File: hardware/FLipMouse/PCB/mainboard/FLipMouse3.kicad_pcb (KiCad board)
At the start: 2 copper layers, 61 x 32 mm, 78 parts, among them J1 PJ320D, J10 Conn_01x06, J13 tp, J14 tp, J15 tp, J16 tp, J17 tp, J2 PJ320D, J3 M50-3900542, J4 Conn_ARM_JTAG_SWD_10, J5 Conn_02x05_Odd_Even, J9 USB_OTG, Q1 BC847, Q2 BSH108, Q3 BC847, Q4 BSH108, Q5 BSH108, Q6 BSH108, SW1 SW_Push, SW2 SW_Push, U1 ESP32-WROOM, U2 TSOP4838, U3 LPC11U14FBD, U4 TSR_1-2433, U5 MPXV7007GP, Y1 JA-12.000-18-DFE

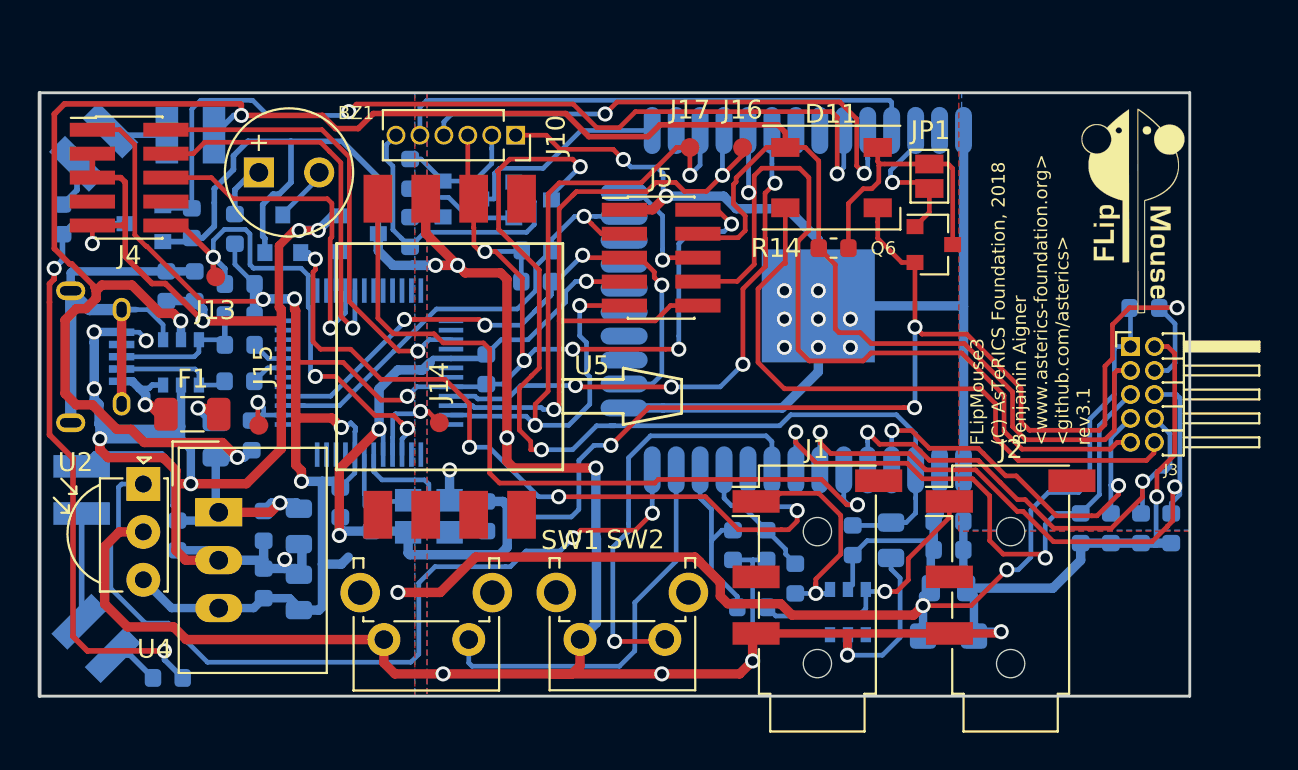
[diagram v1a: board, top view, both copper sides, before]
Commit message: Changed component names for having all part types in one order. Added 3d shapes & beautified silkscreen layers.
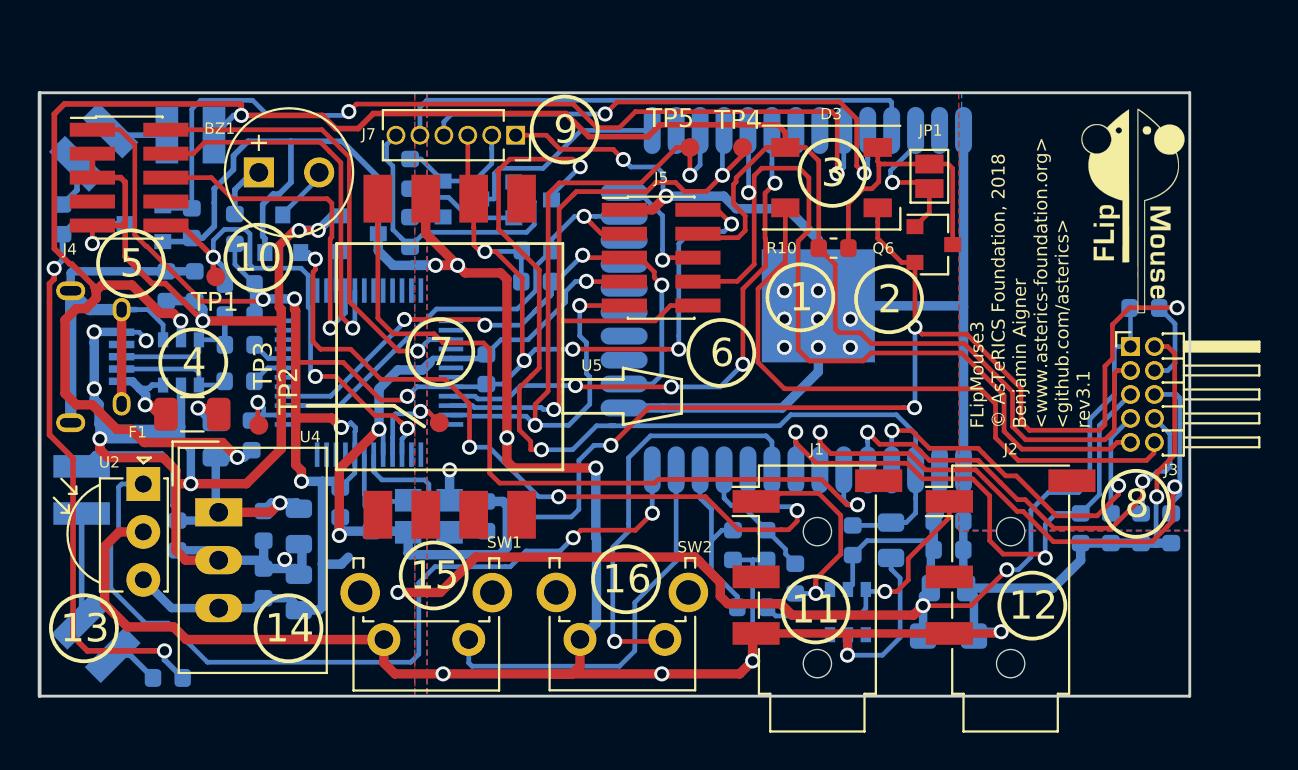
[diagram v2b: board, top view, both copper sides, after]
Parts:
- removed the C14 at (67.3, 141.5)
- removed the C2 at (96.8, 142.0)
- removed J14: tp, Measurement_Points:Measurement_Point_Round-SMD-Pad_Small
- removed the R6 at (120.0, 141.1)
- added C3: 10n, Capacitor_SMD:C_0603_1608Metric, B.Cu at (98.6, 142.0)
- added C4: 10n, Capacitor_SMD:C_0603_1608Metric, B.Cu at (96.8, 142.0)
- added R13: 10k, Resistor_SMD:R_0603_1608Metric, B.Cu at (120.0, 141.1)
- added TP2: tp, Measurement_Points:Measurement_Point_Round-SMD-Pad_Small, F.Cu at (81.2, 135.5)
- C1: value 10n -> 18pF
- C6: value 18pF -> 10n
- R6: renamed from R1; value 1.5k -> 1k5
- R7: renamed from R4; value 1.5k -> 1k5
- moved C6 16.4 mm to (67.3, 141.5)
- moved C1 14.9 mm to (83.7, 140.5), turned to 270 degrees
- renumbered C17 to C10, C23 to C11, C22 to C13, C13 to C14, C19 to C16, C10 to C17, C16 to C18, C8 to C2, C11 to C5, C18 to C7, C20 to C8, C21 to C9, D9 to D1, D3 to D2, D11 to D3, J9 to J6, J10 to J7, Q3 to Q2, Q2 to Q3, R9 to R1, R14 to R10, R17 to R11, R5 to R12, R7 to R14, R8 to R15, R11 to R16, R22 to R17, R10 to R2, R21 to R20, R20 to R21, R12 to R22, R15 to R3, R16 to R4, R3 to R5, R2 to R8, R13 to R9, J13 to TP1, J15 to TP3, J16 to TP4, J17 to TP5
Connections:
- C1 pad 1: GNDD -> GND
- C1 pad 2: /B_1 -> Net-(C1-Pad2)
- C6 pad 1: GND -> VBUS
- C6 pad 2: Net-(C6-Pad2) -> GND
- U3 pad 6: Net-(C6-Pad2) -> Net-(C1-Pad2)
- Y1 pad 1: Net-(C6-Pad2) -> Net-(C1-Pad2)
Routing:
- net Net-(C6-Pad2): track 9.64 -> 0.00 mm
- net Net-(C1-Pad2): track 0.00 -> 9.64 mm
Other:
- board text added: "1"
- board text added: "10"
- board text added: "11"
- board text added: "12"
- board text added: "13"
- board text added: "14"
- board text added: "15"
- board text added: "16"
- board text added: "2"
- board text added: "3"
- board text added: "4"
- board text added: "5"
- board text added: "6"
- board text added: "7"
- board text added: "8"
- board text added: "9"
- board text added: "FLipMouse3 © AsTeRICS Foundation, 2018 Benjamin Aigner <www.asterics-foundation.org> <github.com/asterics> rev3.1"
- board text removed: "FLipMouse3 (C) AsTeRICS Foundation, 2018 Benjamin Aigner <www.asterics-foundation.org> <github.com/asterics> rev3.1"

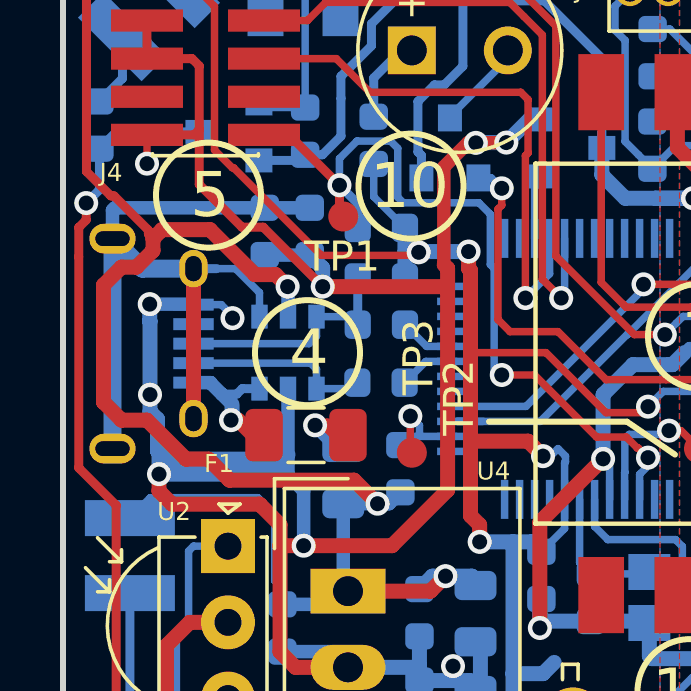
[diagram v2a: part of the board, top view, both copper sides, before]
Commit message: Changed ESD protection for VBUS
Moved the supply voltage pin of suppressor diode array
from VBUS (after fuse & ferrite bead) to the power input of
the USB plug -> ESD protection is bad with an inductor limiting
the ESD diodes.
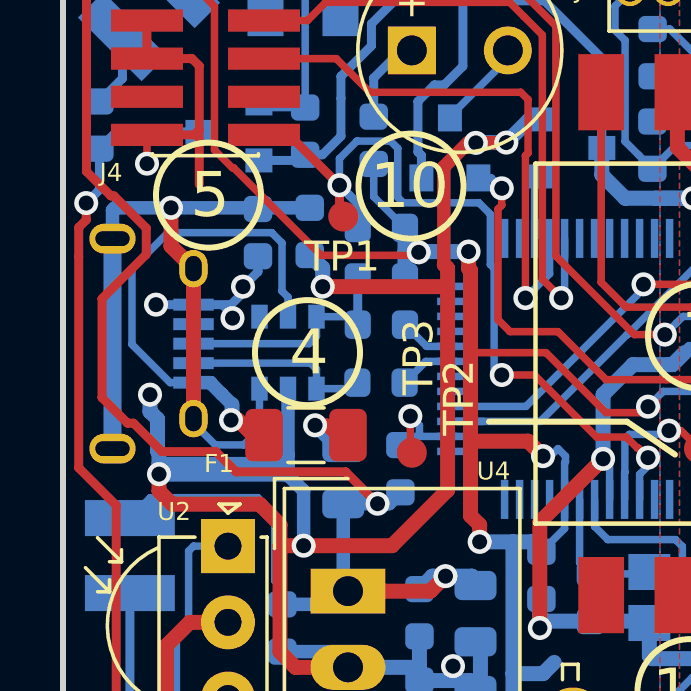
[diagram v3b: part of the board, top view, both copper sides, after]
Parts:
- moved R22 0.23 mm to (66.5, 128.3)
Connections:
- D1 pad 3: Net-(D1-Pad3) -> Net-(C5-Pad2)
- D1 pad 4: Net-(C5-Pad2) -> (no net)
- D1 pad 5: VBUS -> Net-(D1-Pad5)
- F1 pad 2: Net-(D1-Pad3) -> Net-(D1-Pad5)
- J6 pad 1: Net-(D1-Pad3) -> Net-(D1-Pad5)
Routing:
- net Net-(D1-Pad5): track 0.00 -> 16.8 mm, vias 0 -> 1
- net VBUS: track 142.5 -> 135.6 mm, vias 4 -> 3
- net GND: track 203.9 -> 197.1 mm, vias 18 -> 19
- net Net-(D1-Pad3): track 4.88 -> 0.00 mm, vias 1 -> 0
- net Net-(C5-Pad2): vias 0 -> 1

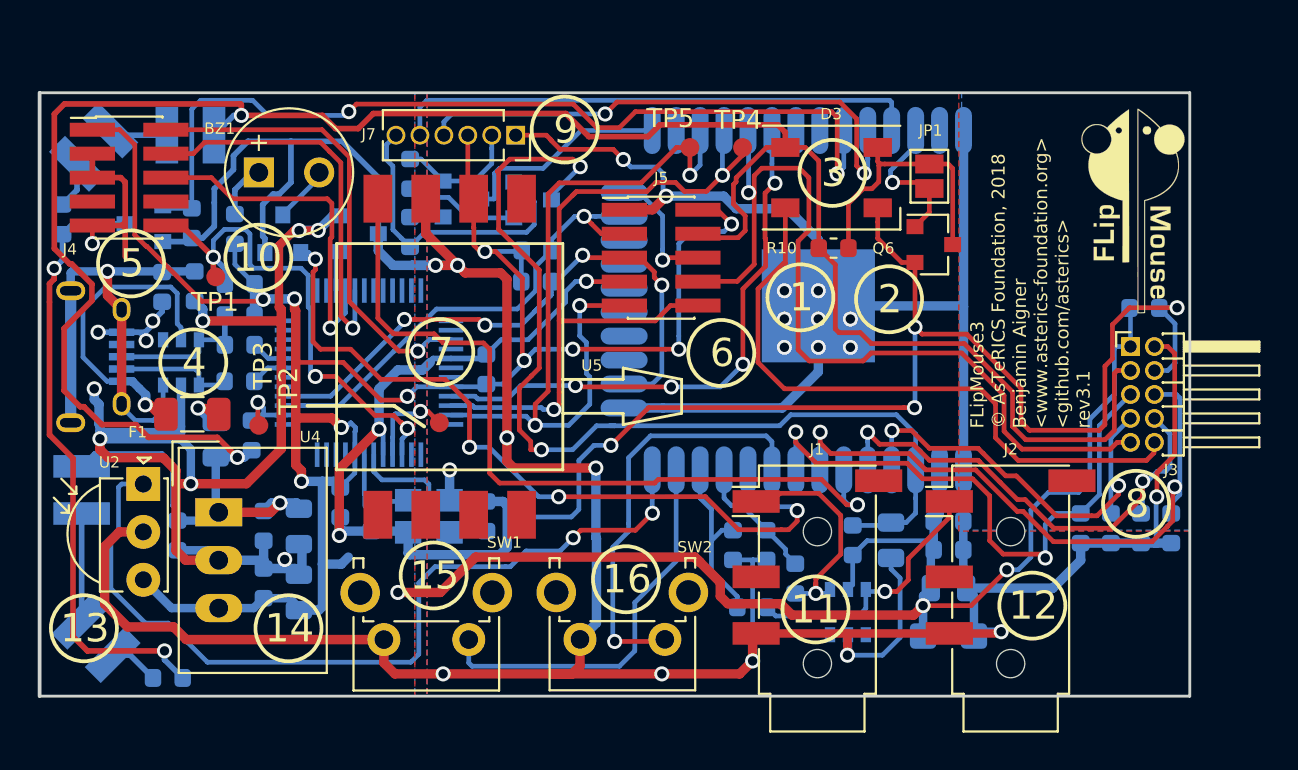
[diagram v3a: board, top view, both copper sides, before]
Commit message: Production ready, alpha: * Added marks/logos/fiducials * Changed neopixel driving * Moved RX/TX of EXT header from internal UART to free pins * Renumbered all parts for having same part types with following numbers * Added PDFs of PCB
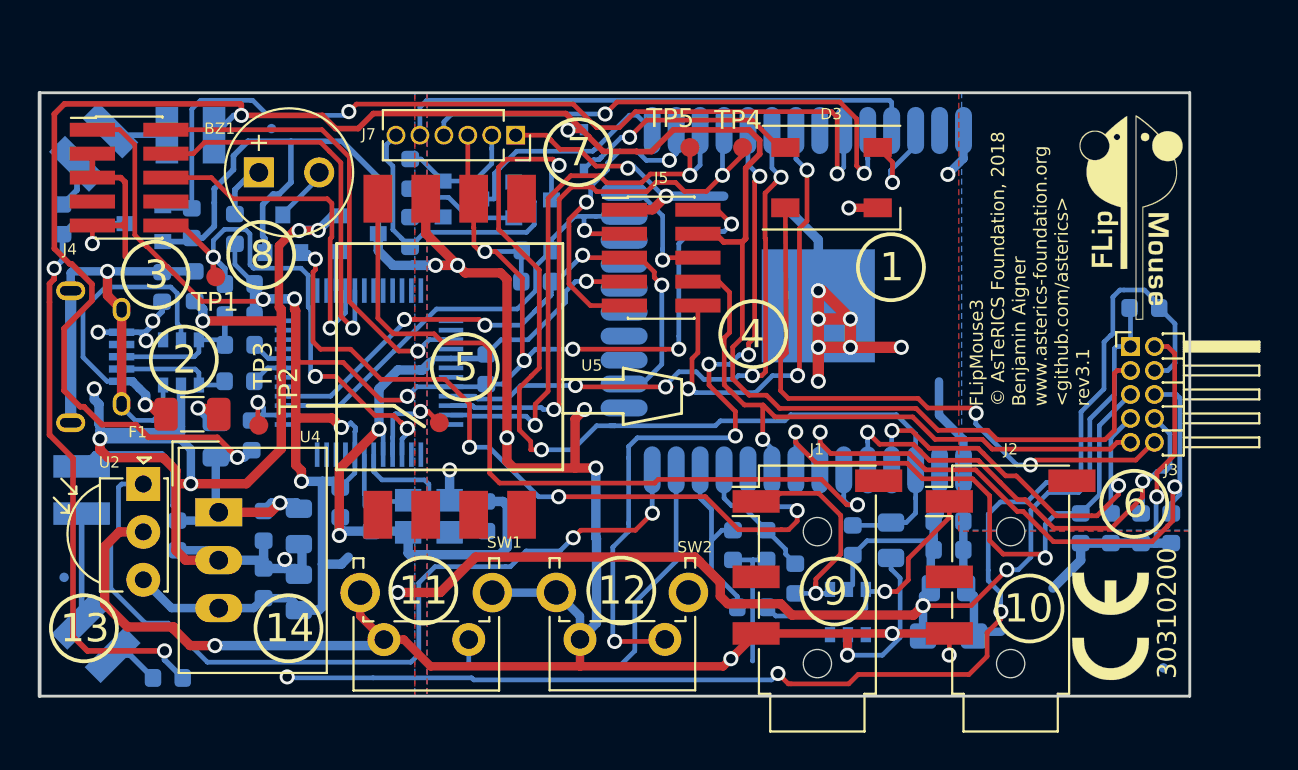
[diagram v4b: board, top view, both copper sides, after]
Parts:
- removed G***: LOGO, Logo:flipmouse_11x5
- removed JP1: IO direct, Jumper:SolderJumper-2_P1.3mm_Open_Pad1.0x1.5mm
- removed Q6: BSH108, Package_TO_SOT_SMD:SOT-23
- removed the R10 at (102.1, 126.2)
- added D8: 1N4148WS, Diode_SMD:D_SOD-323, B.Cu at (88.9, 121.0)
- added FID1: Fiducial, Fiducial:Fiducial_0.5mm_Dia_1mm_Outer, B.Cu at (119.6, 148.5)
- added FID2: Fiducial, Fiducial:Fiducial_0.5mm_Dia_1mm_Outer, B.Cu at (61.3, 143.7)
- added FID3: Fiducial, Fiducial:Fiducial_0.5mm_Dia_1mm_Outer, B.Cu at (72.3, 119.9)
- added LOGO1: Logo_FLipMouse, Logo:flipmouse_11x5, F.Cu at (117.9, 124.6)
- added LOGO2: Logo_WEEE, Symbol:WEEE-Logo_4.2x6mm_SilkScreen, B.Cu at (117.4, 146.0)
- added LOGO3: Logo_CE, Logo:CE, F.Cu at (116.8, 146.3)
- C18: value 100uF -> 15uF
- R1, R2: value 22R,min 0.125W -> 15R,min 0.125W
- renumbered R11 to R10, R21 to R11, R22 to R21
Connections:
- D3 pad 1: GND -> GNDD
- D3 pad 3: VBUS -> Net-(D3-Pad3)
- J5 pad 10: /ESP_TX -> /EXT_RX
- J5 pad 9: /ESP_RX -> /EXT_TX
- SW1 pad : (no net) -> GNDD
- SW2 pad : (no net) -> GNDD
- U1 pad 26: (no net) -> /EXT_TX
- U1 pad 29: /EXT1 -> /B_0
- U1 pad 31: (no net) -> /EXT_RX
- U1 pad 36: Net-(JP1-Pad1) -> /LED1
- U1 pad 9: /B_0 -> /EXT1
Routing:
- net GNDD: track 254.1 -> 229.0 mm, vias 20 -> 22
- net /EXT_RX: track 0.00 -> 24.4 mm, vias 0 -> 3
- net /EXT_TX: track 0.00 -> 17.4 mm, vias 0 -> 2
- net /B_0: track 22.5 -> 38.4 mm, vias 1 -> 5
- net Net-(D3-Pad3): track 0.00 -> 12.5 mm, vias 0 -> 1
- net /EXT1: track 45.7 -> 33.8 mm
- net /ESP_RX: track 41.0 -> 29.5 mm, vias 3 -> 2
- net /LED1: track 14.3 -> 5.49 mm, vias 0 -> 1
- net Net-(JP1-Pad1): track 7.84 -> 0.00 mm, vias 1 -> 0
- net /ESP_TX: track 38.3 -> 30.9 mm
- net GND: track 197.1 -> 201.4 mm, vias 19 -> 18
- net /LED2: track 33.8 -> 32.2 mm, vias 0 -> 2
- net /ESP_SIGNAL: track 29.8 -> 31.4 mm
- net /E_RESET: track 53.2 -> 52.0 mm
- net VBUS: track 135.6 -> 134.6 mm, vias 3 -> 4
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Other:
- board text added: "30310200"
- board text added: "FLipMouse3 © AsTeRICS Foundation, 2018 Benjamin Aigner www.asterics-foundation.org <github.com/asterics> rev3.1"
- board text added: "RoHS"
- board text removed: "15"
- board text removed: "16"
- board text removed: "FLipMouse3 © AsTeRICS Foundation, 2018 Benjamin Aigner <www.asterics-foundation.org> <github.com/asterics> rev3.1"

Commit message: Improvements&fixes: * Replaced PJ320D (china jack plugs) with plugs from digikey (RoHS!) * Added remaining 3D shapes to PCB * Removed GND from unused jack plug pins (might result in unusable buttons because of mono cables)
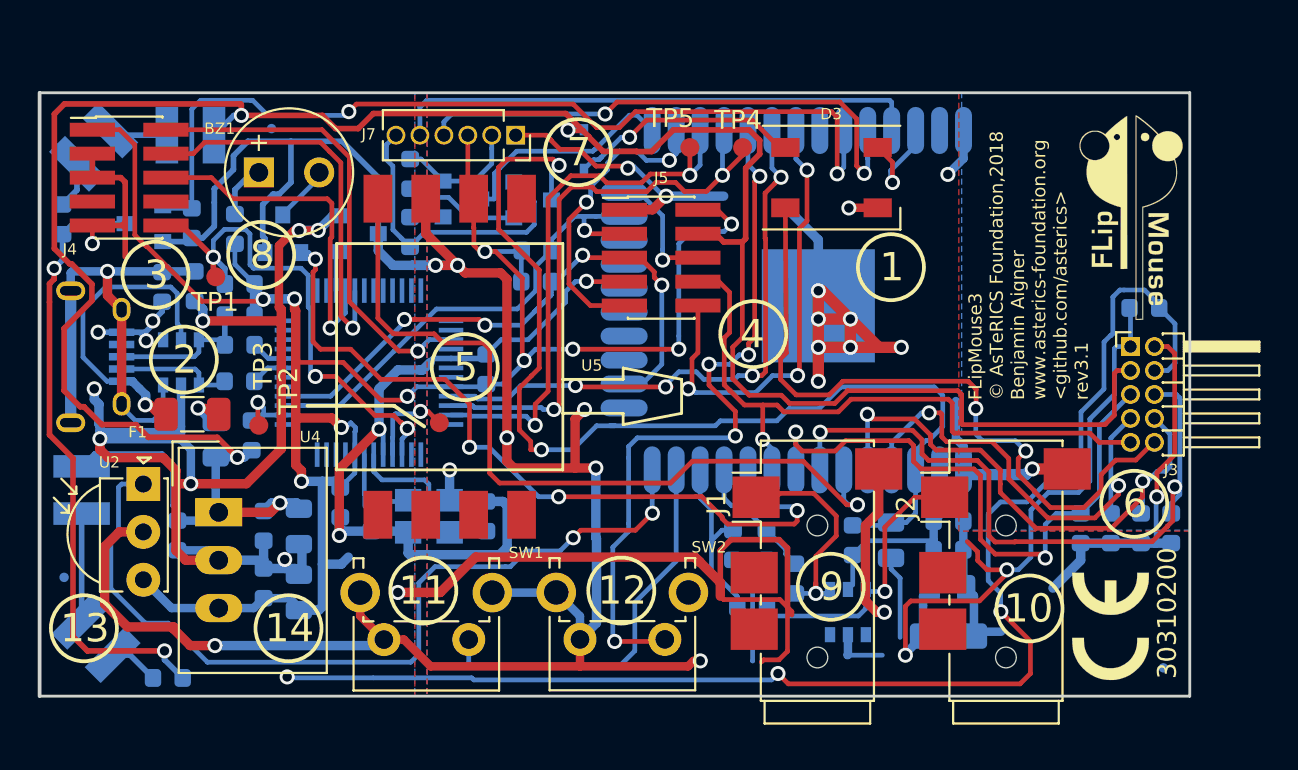
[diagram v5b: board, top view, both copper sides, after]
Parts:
- J1, J2: value PJ320D -> SJ2-3574A; footprint Connector_Audio:Jack_3.5mm_PJ320D_Horizontal -> JackPlug:Jack_3.5mm_SJ2-357X
- moved J2 6.75 mm to (111.2, 150.2)
- moved J1 6.75 mm to (101.2, 150.2)
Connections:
- J1 pad 1: Net-(D2-Pad4) -> GNDD
- J1 pad 2: (no net) -> Net-(D2-Pad4)
- J1 pad 3: GNDD -> (no net)
- J2 pad 1: Net-(D2-Pad6) -> GNDD
- J2 pad 2: (no net) -> Net-(D2-Pad6)
- J2 pad 3: GNDD -> (no net)
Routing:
- net +3V3: track 183.3 -> 197.8 mm
- net /LED2: track 32.2 -> 37.2 mm
- net /E_RESET: track 52.0 -> 56.5 mm
- net /FSR3: track 22.7 -> 26.6 mm
- net GND: track 201.4 -> 204.6 mm
- net GNDD: track 229.0 -> 225.9 mm, vias 22 -> 21
- net /FSR4: track 26.2 -> 28.6 mm
- net /FSR2: track 33.8 -> 36.0 mm
- net /FSR1: track 31.0 -> 32.6 mm
- net /EXT1: track 33.8 -> 34.9 mm
- net /PRESSURE: track 42.3 -> 43.1 mm
- net Net-(D2-Pad6): track 14.2 -> 14.9 mm
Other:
- board text added: "FLipMouse3 © AsTeRICS Foundation,2018 Benjamin Aigner www.asterics-foundation.org <github.com/asterics> rev3.1"
- board text removed: "FLipMouse3 © AsTeRICS Foundation, 2018 Benjamin Aigner www.asterics-foundation.org <github.com/asterics> rev3.1"

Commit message: Changed USB chipset to LPC11U__2__4 (from LPC11U14): This introduces the possibility to use the USB-MSD bootloader for software updates. Otherwise we would need either a serial adapter, a custom bootloader or a programming software within the ESP32 (and more nets between these two chips).
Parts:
- U3: value LPC11U14FBD -> LPC11U24FBD
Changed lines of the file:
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@@
     (fp_line (start 4 -8.35) (end 4 -2.59) (layer F.Fab) (width 0.1))
     (fp_line (start 0.5 -8.35) (end 0.5 -2.59) (layer F.Fab) (width 0.1))
-    (pad "" thru_hole circle (at -1.25 2.49 180) (size 2.1 2.1) (drill 1.3) (layers *.Cu *.Mask)
-      (net 4 GNDD))
+    (pad "" thru_hole circle (at -1.25 2.49 180) (size 2.1 2.1) (drill 1.3) (layers *.Cu *.Mask))
     (pad 1 thru_hole circle (at 0 0 180) (size 1.75 1.75) (drill 0.99) (layers *.Cu *.Mask)
       (net 3 /B_0))
@@
       (effects (font (size 0.6 0.6) (thickness 0.15)) (justify mirror))
     )
-    (fp_text value LPC11U14FBD (at 0 -6 90) (layer B.Fab)
-      (effects (font (size 1 1) (thickness 0.15)) (justify mirror))
-    )
+    (fp_text value LPC11U24FBD (at 0 -6 90) (layer B.Fab)
+      (effects (font (size 1 1) (thickness 0.15)) (justify mirror))
+    )
